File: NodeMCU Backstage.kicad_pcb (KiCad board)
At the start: 2 copper layers, 31.8 x 54.9 mm, 9 parts, among them CON1 BARREL_JACK_NO_SW, Q1 BSS138, U1 R-78E5.0-0.5, U2 NODEMCU_AMICA, U3 HEADER_WS2812

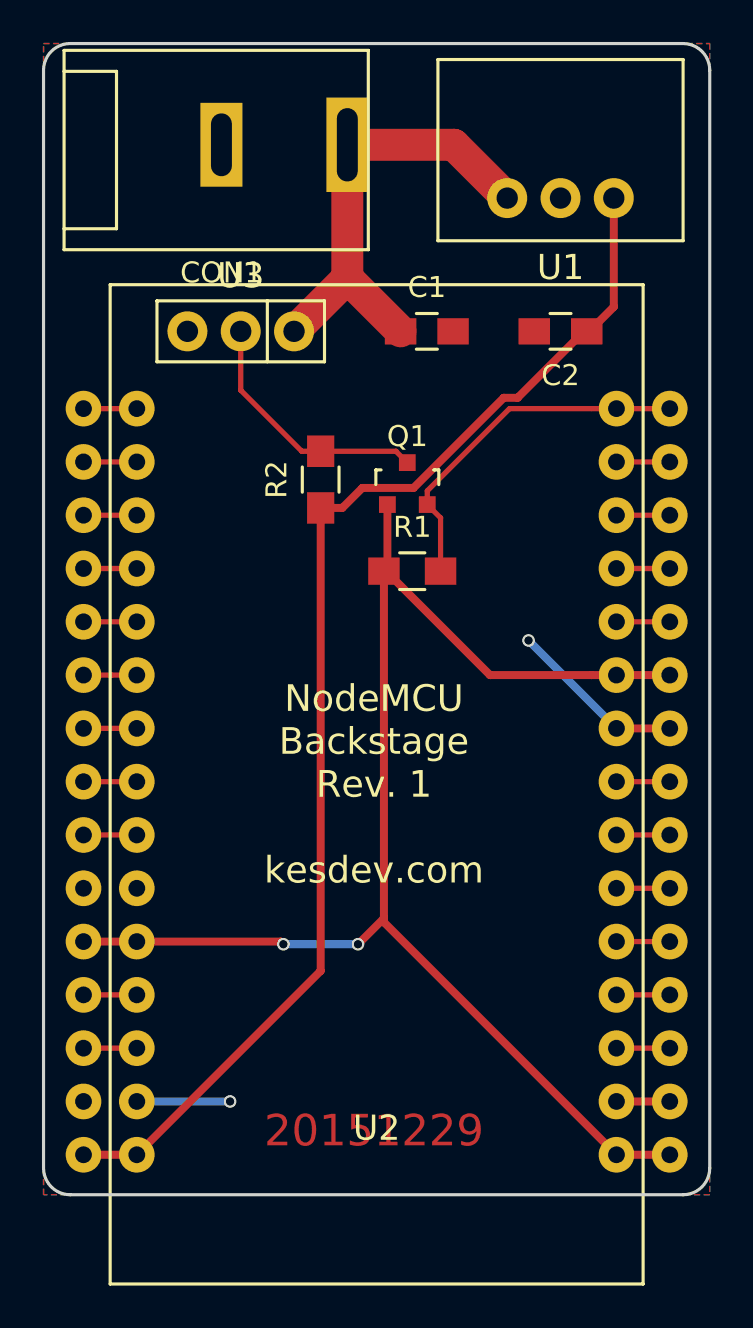
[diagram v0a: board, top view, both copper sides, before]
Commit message: rev2: better silk labels, switch to vias not slot barrel solder
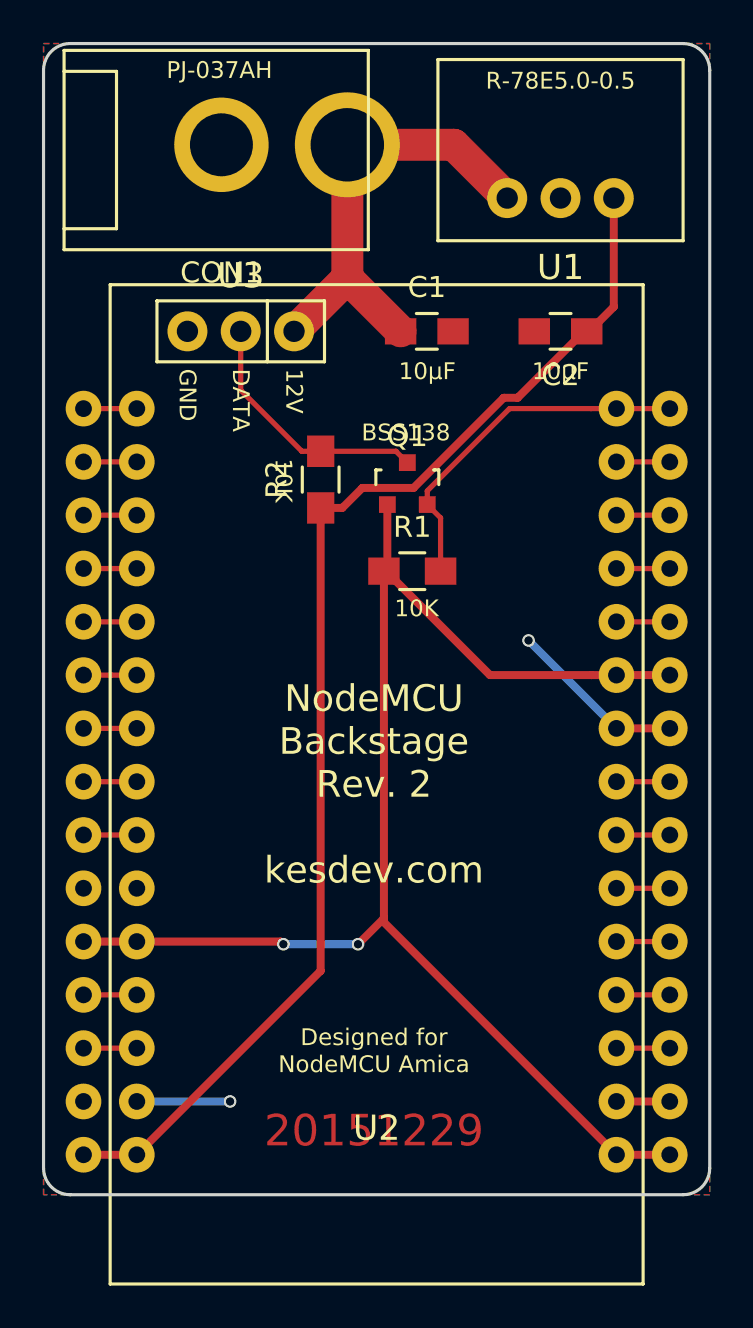
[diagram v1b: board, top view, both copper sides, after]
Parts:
- CON1: footprint mplewis:PJ-037A -> mplewis:PJ-037A-VIAS
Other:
- rule pad_to_mask_clearance: 0.2 -> 0
- board text added: "10K"
- board text added: "10µF"
- board text added: "12V"
- board text added: "BSS138"
- board text added: "DATA"
- board text added: "Designed for NodeMCU Amica"
- board text added: "GND"
- board text added: "NodeMCU Backstage Rev. 2 kesdev.com"
- board text added: "PJ-037AH"
- board text added: "R-78E5.0-0.5"
- board text removed: "NodeMCU Backstage Rev. 1 kesdev.com"
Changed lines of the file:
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@@
     (area 34.976999 28.935 66.877001 90.127501)
     (thickness 1.6)
-    (drawings 10)
+    (drawings 22)
     (tracks 80)
     (zones 0)
@@
     (pad_size 1.524 1.524)
     (pad_drill 0.762)
-    (pad_to_mask_clearance 0.2)
+    (pad_to_mask_clearance 0)
+    (pad_to_paste_clearance -0.003)
     (aux_axis_origin 0 0)
-    (visible_elements FFFFFF7F)
+    (visible_elements FFFCFF7F)
     (pcbplotparams
-      (layerselection 0x010e0_80000001)
+      (layerselection 0x010f0_80000001)
       (usegerberextensions true)
       (excludeedgelayer true)
@@
       (net 4 "Net-(Q1-Pad2)"))
   )
-  (module mplewis:PJ-037A (layer F.Cu)
-    (at 43.53 35.56)
-    (fp_text reference CON1 (at 0 6.096) (layer F.SilkS)
-      (effects (font (size 1 1) (thickness 0.15)))
-    )
-    (fp_text value BARREL_JACK_NO_SW (at 0 -5.5) (layer F.Fab)
-      (effects (font (size 1 1) (thickness 0.15)))
-    )
-    (fp_line (start -7.5 -3.5) (end -5 -3.5) (layer F.SilkS) (width 0.15))
-    (fp_line (start -5 -3.5) (end -5 4) (layer F.SilkS) (width 0.15))
-    (fp_line (start -5 4) (end -7.5 4) (layer F.SilkS) (width 0.15))
-    (fp_line (start -7.5 5) (end -7.5 -4.5) (layer F.SilkS) (width 0.15))
-    (fp_line (start 7 5) (end -7.5 5) (layer F.SilkS) (width 0.15))
-    (fp_line (start 7 -4.5) (end 7 5) (layer F.SilkS) (width 0.15))
-    (fp_line (start -7.5 -4.5) (end 7 -4.5) (layer F.SilkS) (width 0.15))
-    (pad 2 thru_hole rect (at 0 0) (size 2 4) (drill oval 1 3) (layers *.Cu *.Mask F.SilkS)
-      (net 1 GND))
-    (pad 1 thru_hole rect (at 6 0) (size 2 4.5) (drill oval 1 3.5) (layers *.Cu *.Mask F.SilkS)
-      (net 2 +12V))
-  )
   (module SOT-23 (layer F.Cu)
     (at 52.39 51.70424)
@@
     )
   )
+  (module mplewis:PJ-037A-VIAS (layer F.Cu)
+    (at 43.53 35.56)
+    (fp_text reference CON1 (at 0 6.096) (layer F.SilkS)
+      (effects (font (size 1 1) (thickness 0.15)))
+    )
+    (fp_text value BARREL_JACK_NO_SW (at 0 -5.5) (layer F.Fab)
+      (effects (font (size 1 1) (thickness 0.15)))
+    )
+    (fp_line (start -7.5 -3.5) (end -5 -3.5) (layer F.SilkS) (width 0.15))
+    (fp_line (start -5 -3.5) (end -5 4) (layer F.SilkS) (width 0.15))
+    (fp_line (start -5 4) (end -7.5 4) (layer F.SilkS) (width 0.15))
+    (fp_line (start -7.5 5) (end -7.5 -4.5) (layer F.SilkS) (width 0.15))
+    (fp_line (start 7 5) (end -7.5 5) (layer F.SilkS) (width 0.15))
+    (fp_line (start 7 -4.5) (end 7 5) (layer F.SilkS) (width 0.15))
+    (fp_line (start -7.5 -4.5) (end 7 -4.5) (layer F.SilkS) (width 0.15))
+    (pad 2 thru_hole circle (at 0 0) (size 4.5 4.5) (drill 3) (layers *.Cu *.Mask F.SilkS)
+      (net 1 GND))
+    (pad 1 thru_hole circle (at 6 0) (size 5 5) (drill 3.5) (layers *.Cu *.Mask F.SilkS)
+      (net 2 +12V))
+  )
+  (gr_text R-78E5.0-0.5 (at 59.69 32.512) (layer F.SilkS)
+    (effects (font (size 0.8 0.8) (thickness 0.1)))
+  )
+  (gr_text PJ-037AH (at 43.434 32.004) (layer F.SilkS)
+    (effects (font (size 0.8 0.8) (thickness 0.1)))
+  )
+  (gr_text "Designed for\nNodeMCU Amica" (at 50.8 78.74) (layer F.SilkS)
+    (effects (font (size 0.8 0.8) (thickness 0.1)))
+  )
+  (gr_text GND (at 41.91 46.228 270) (layer F.SilkS)
+    (effects (font (size 0.8 0.8) (thickness 0.1)) (justify left))
+  )
+  (gr_text DATA (at 44.45 46.228 270) (layer F.SilkS)
+    (effects (font (size 0.8 0.8) (thickness 0.1)) (justify left))
+  )
+  (gr_text 12V (at 46.99 46.228 270) (layer F.SilkS)
+    (effects (font (size 0.8 0.8) (thickness 0.1)) (justify left))
+  )
+  (gr_text 10K (at 52.832 57.658 360) (layer F.SilkS)
+    (effects (font (size 0.8 0.8) (thickness 0.1)))
+  )
+  (gr_text 10K (at 46.482 51.562 270) (layer F.SilkS)
+    (effects (font (size 0.8 0.8) (thickness 0.1)))
+  )
+  (gr_text BSS138 (at 52.324 49.276) (layer F.SilkS)
+    (effects (font (size 0.8 0.8) (thickness 0.1)))
+  )
+  (gr_text 10µF (at 59.69 46.355) (layer F.SilkS)
+    (effects (font (size 0.8 0.8) (thickness 0.1)))
+  )
+  (gr_text 10µF (at 53.34 46.355) (layer F.SilkS)
+    (effects (font (size 0.8 0.8) (thickness 0.1)))
+  )
+  (gr_text "NodeMCU\nBackstage\nRev. 2\n\nkesdev.com" (at 50.8 66.04) (layer B.SilkS)
+    (effects (font (thickness 0.254)) (justify mirror))
+  )
   (gr_line (start 65.532 30.734) (end 36.322 30.734) (layer Edge.Cuts) (width 0.15))
   (gr_line (start 66.802 84.328) (end 66.802 32.004) (layer Edge.Cuts) (width 0.15))
@@
     (effects (font (size 1.5 1.5) (thickness 0.3)))
   )
-  (gr_text "NodeMCU\nBackstage\nRev. 1\n\nkesdev.com" (at 50.8 66.04) (layer F.SilkS)
+  (gr_text "NodeMCU\nBackstage\nRev. 2\n\nkesdev.com" (at 50.8 66.04) (layer F.SilkS)
     (effects (font (thickness 0.254)))
   )
